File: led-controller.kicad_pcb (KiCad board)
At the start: 2 copper layers, 100 x 67 mm, 87 parts, among them J1 STLINK, J2 PWR, J3 GRP1, J4 GRP2, J5 GRP3, J6 GRP4, J7 SWITCH, Q1 Q_NMOS_GSD, Q10 Q_NMOS_GSD, Q11 Q_NMOS_GSD, Q12 Q_NMOS_GSD, Q13 DMP4015SK3, Q2 Q_NMOS_GSD, Q3 Q_NMOS_GSD, Q4 Q_NMOS_GSD, Q5 Q_NMOS_GSD, Q6 Q_NMOS_GSD, Q7 Q_NMOS_GSD, Q8 Q_NMOS_GSD, Q9 Q_NMOS_GSD, SW1 SW_Push, U1 STM32F101C8Tx, U2 LTV-814, U3 MCP16301, U4 ATWINC15x0, U5 24LC16

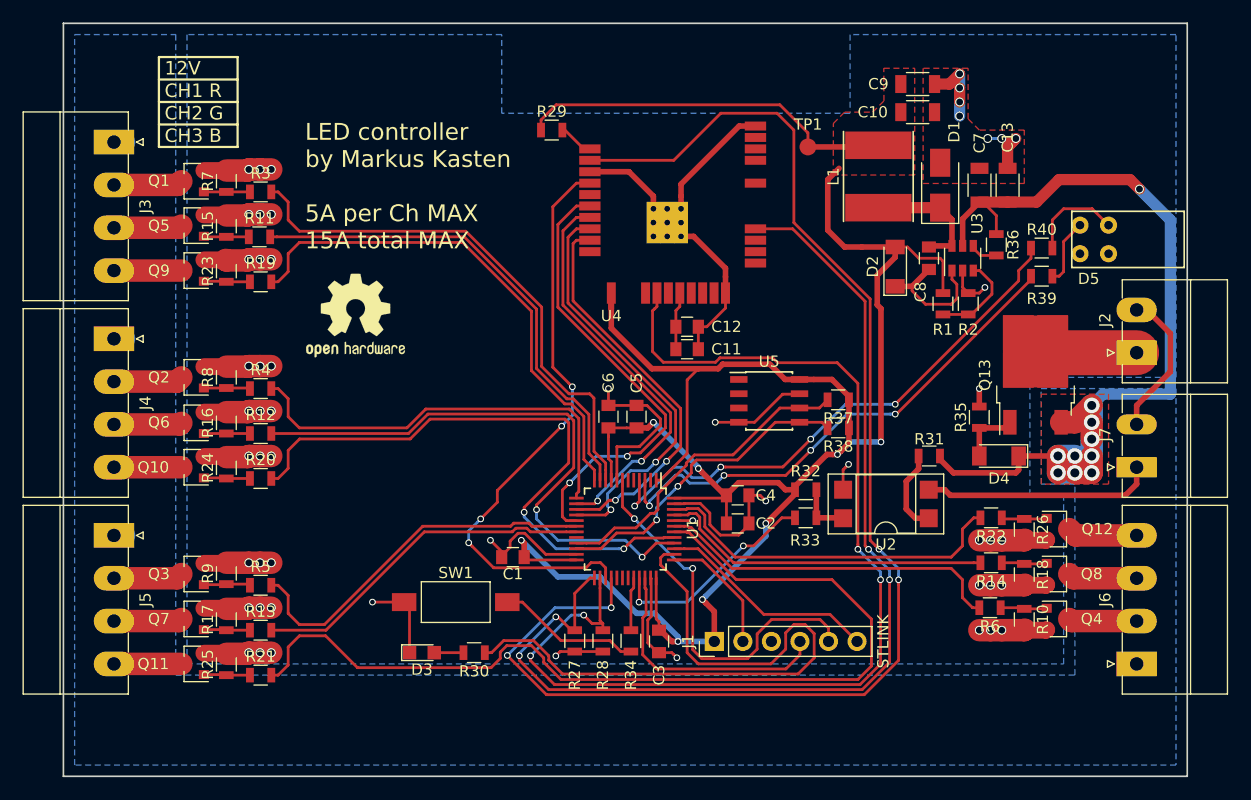
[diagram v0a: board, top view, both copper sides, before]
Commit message: Add UART headers for mcu and winc
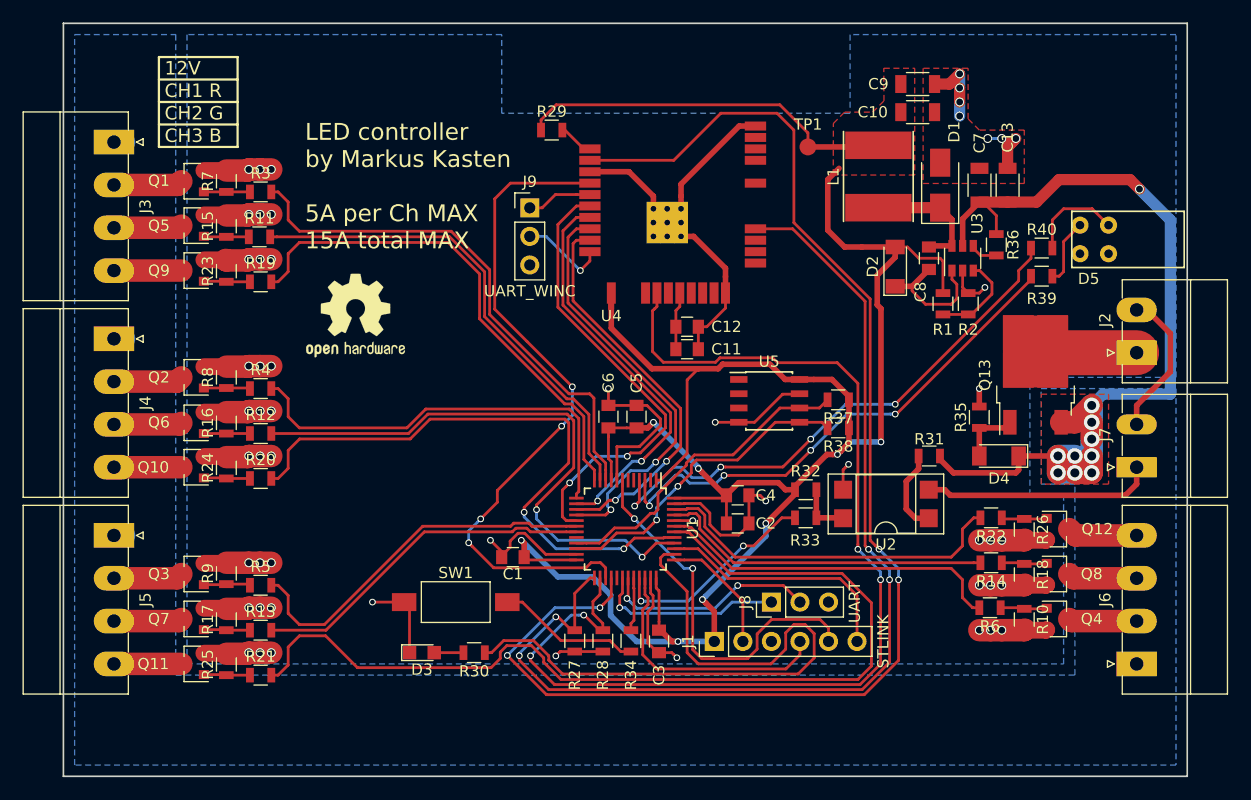
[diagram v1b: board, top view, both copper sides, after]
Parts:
- added J8: UART, Pin_Headers:Pin_Header_Straight_1x03_Pitch2.54mm, F.Cu at (183.0, 84.5)
- added J9: UART_WINC, Pin_Headers:Pin_Header_Straight_1x03_Pitch2.54mm, F.Cu at (161.5, 49.4)
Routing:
- net /MCU/UART_RX: track 0.00 -> 19.1 mm, vias 0 -> 2
- net /MCU/UART_TX: track 0.00 -> 16.9 mm, vias 0 -> 1
- net /ethernet/UART_RX: track 0.00 -> 7.79 mm, vias 0 -> 1
- net /MCU/ETH_IRQ: track 53.0 -> 60.7 mm
- net /ethernet/UART_TX: track 0.00 -> 5.84 mm
- net /MCU/SWO: track 19.7 -> 22.1 mm
- net /LED_driver/CH9: track 85.0 -> 85.9 mm
- net +3V3: track 211.8 -> 212.6 mm
- net /ethernet/ENABLE: track 97.2 -> 97.9 mm
- net /LED_driver/CH3: track 45.8 -> 45.0 mm
- net /LED_driver/CH2: track 44.3 -> 43.5 mm
- net /LED_driver/CH1: track 48.1 -> 47.3 mm
- net /MCU/ETH_WAKE: track 122.7 -> 122.1 mm

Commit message: Add license to silkscreen layer
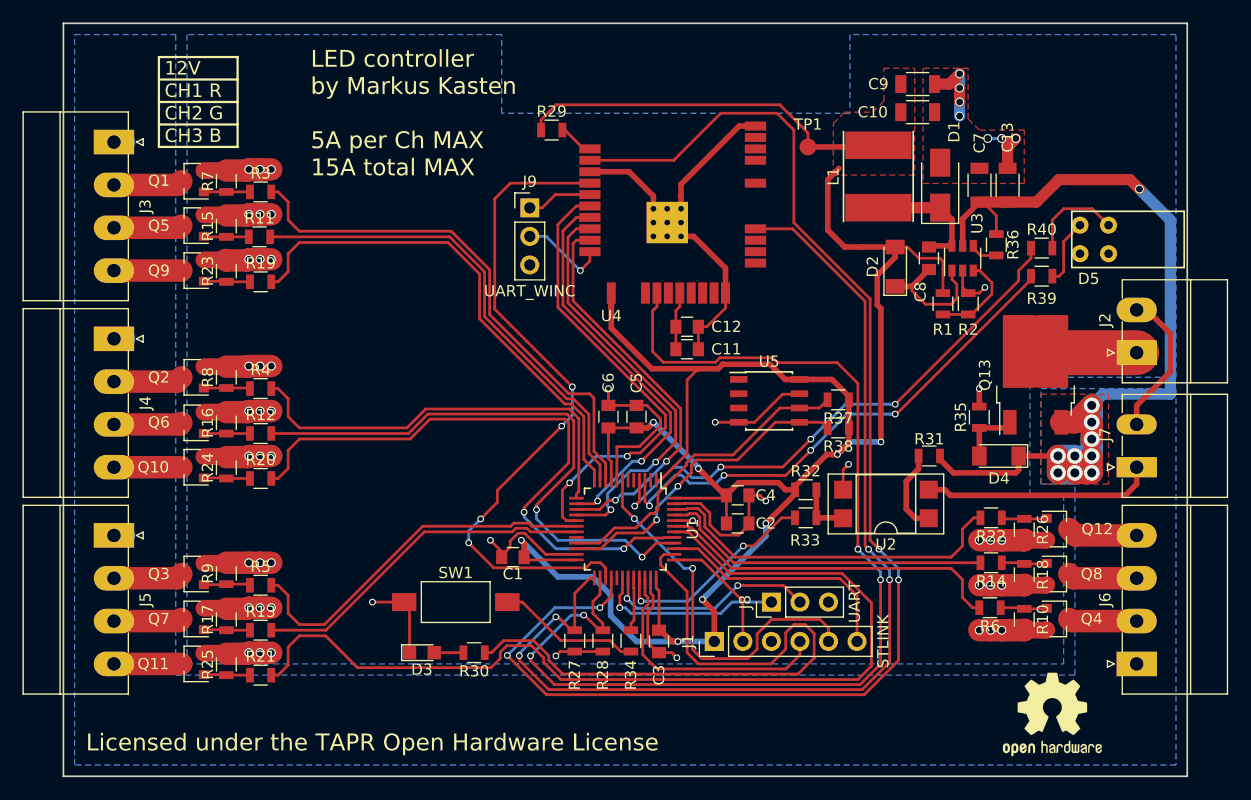
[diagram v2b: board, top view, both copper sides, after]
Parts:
- moved REF*** 71.4 mm to (208.0, 94.5)
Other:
- board text added: "Licensed under the TAPR Open Hardware License"
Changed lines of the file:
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@@
   (general
     (links 204)
-    (no_connects 5)
+    (no_connects 0)
     (area 119.924999 32.924999 220.075001 100.075001)
     (thickness 1.6)
-    (drawings 24)
+    (drawings 25)
     (tracks 1014)
     (zones 0)
@@
     (pad_drill 1.2)
     (pad_to_mask_clearance 0.2)
+    (solder_mask_min_width 0.3)
     (aux_axis_origin 0 0)
     (visible_elements FFFFFFFF)
     (pcbplotparams
-      (layerselection 0x00030_80000001)
-      (usegerberextensions false)
+      (layerselection 0x010f0_80000001)
+      (usegerberextensions true)
       (excludeedgelayer true)
       (linewidth 0.100000)
@@
       (drillshape 0)
       (scaleselection 1)
-      (outputdirectory ""))
+      (outputdirectory gerber/))
   )
   (net 0 "")
@@
   )
   (module Symbols:OSHW-Logo2_9.8x8mm_SilkScreen (layer F.Cu)
-    (at 146 59)
+    (at 208 94.5)
     (descr "Open Source Hardware Symbol")
     (tags "Logo Symbol OSHW")
@@
     )
   )
+  (gr_text "Licensed under the TAPR Open Hardware License" (at 122 97) (layer F.SilkS)
+    (effects (font (size 1.5 1.5) (thickness 0.3)) (justify left))
+  )
   (dimension 25 (width 0.3) (layer Dwgs.User)
     (gr_text "25.000 mm" (at 236.35 52.5 90) (layer Dwgs.User)
@@
   (gr_line (start 128.5 44) (end 135.5 44) (layer F.SilkS) (width 0.2))
   (gr_line (start 128.5 36) (end 128.5 44) (layer F.SilkS) (width 0.2))
-  (gr_text "LED controller\nby Markus Kasten\n\n5A per Ch MAX\n15A total MAX" (at 141.5 47.5) (layer F.SilkS)
+  (gr_text "LED controller\nby Markus Kasten\n\n5A per Ch MAX\n15A total MAX" (at 142 41) (layer F.SilkS)
     (effects (font (size 1.5 1.5) (thickness 0.3)) (justify left))
   )

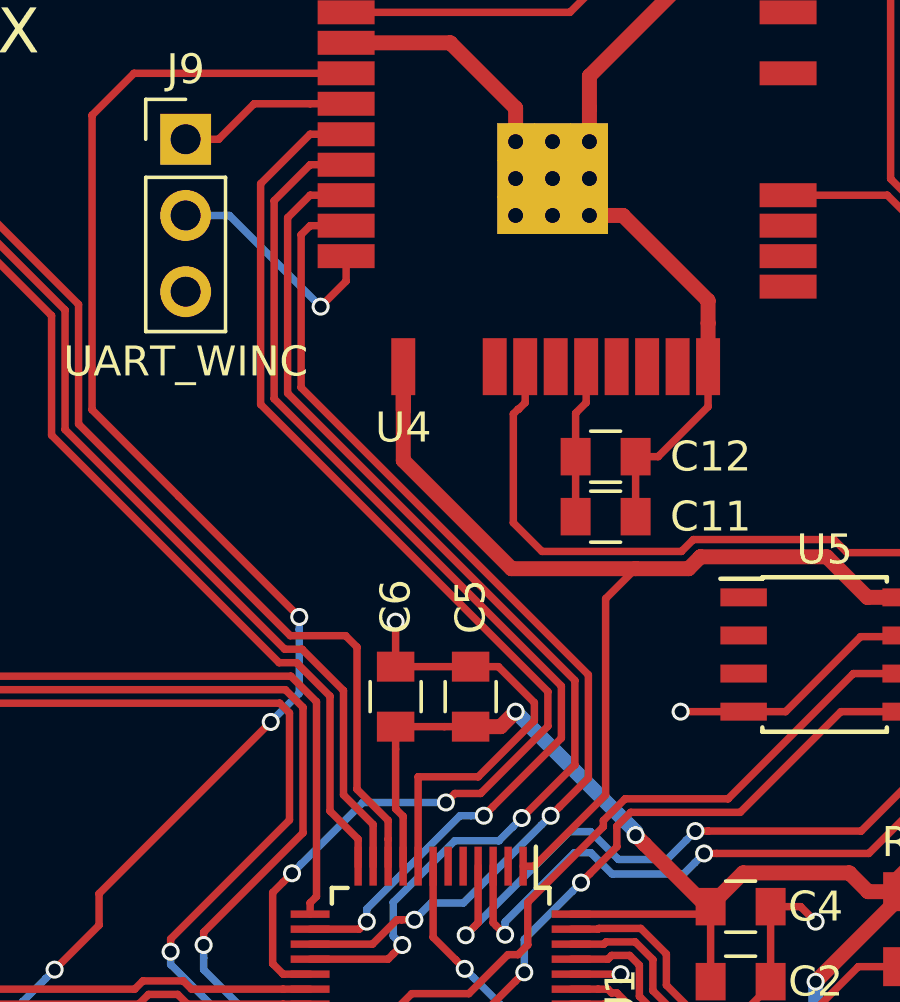
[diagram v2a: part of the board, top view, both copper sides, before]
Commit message: Fix wrong pin in ATWINC symbol and add a cap to it's VCC
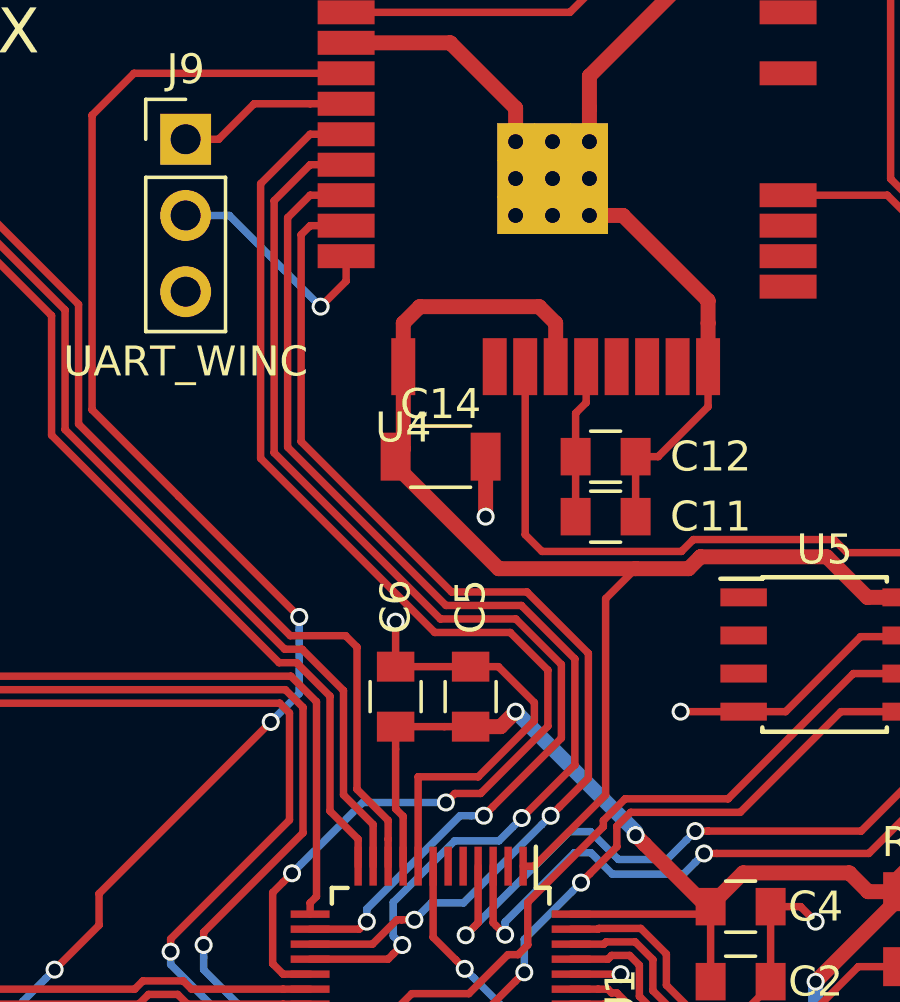
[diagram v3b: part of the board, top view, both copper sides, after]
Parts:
- added C14: 10u, Capacitors_SMD:C_1206, F.Cu at (170.0, 60.0)
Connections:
- U4 pad 23: Net-(U4-Pad23) -> +3V3
- U4 pad 25: (no net) -> Net-(U4-Pad25)
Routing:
- net +3V3: track 212.6 -> 220.5 mm
- net GND: track 210.0 -> 212.0 mm, vias 54 -> 55
- net /MCU/SPI_SCK: track 35.3 -> 36.7 mm
- net /MCU/SPI_MISO: track 37.2 -> 38.7 mm
- net /MCU/SPI_CS: track 36.0 -> 37.5 mm
- net /MCU/SPI_MOSI: track 40.8 -> 42.3 mm

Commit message: Some final silkscreen fixes
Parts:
- added REF***: KiCad-Logo2_6mm_SilkScreen, Symbols:KiCad-Logo2_6mm_SilkScreen, F.Cu at (206.0, 95.0)
- moved REF*** 14.0 mm to (194.0, 94.5)
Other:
- board text added: "LED controller by Markus Kasten rev 1.0 5A per Ch MAX 15A total MAX"
- board text removed: "LED controller by Markus Kasten 5A per Ch MAX 15A total MAX"
